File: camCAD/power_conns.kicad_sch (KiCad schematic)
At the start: 3 parts, among them J3 BATTERY

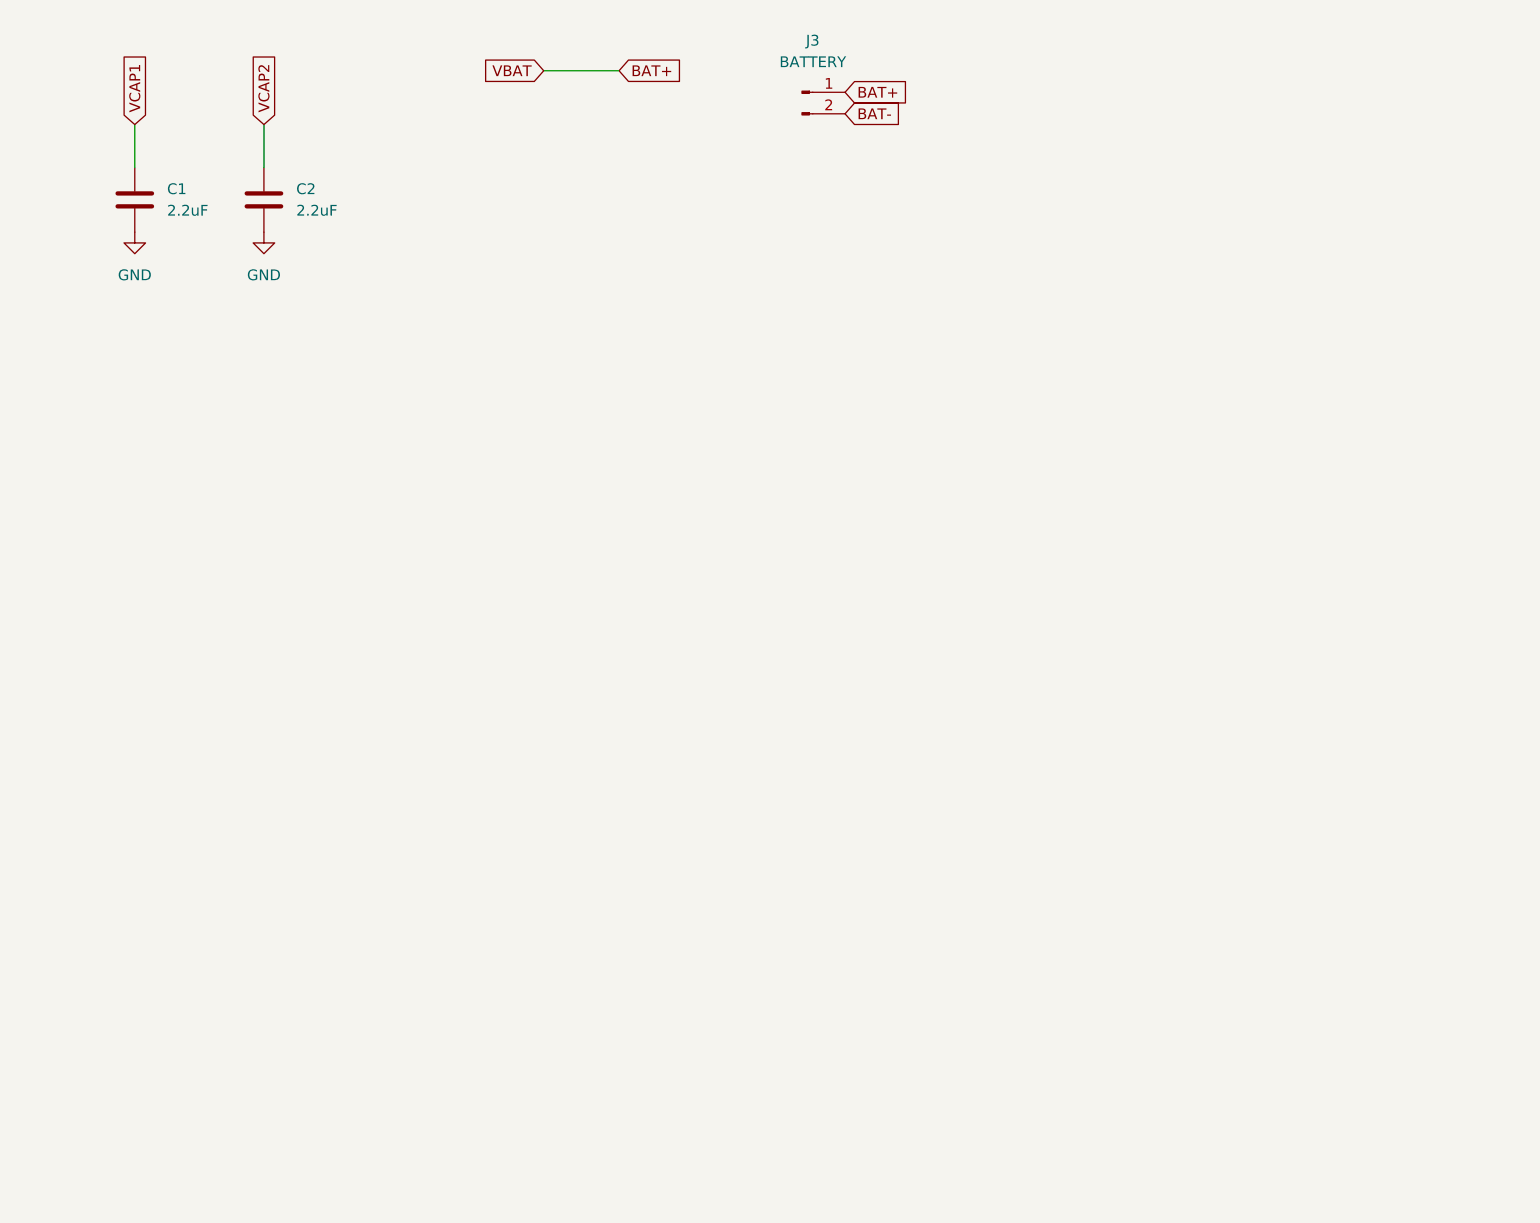
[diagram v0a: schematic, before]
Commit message: Included buck converter schematic
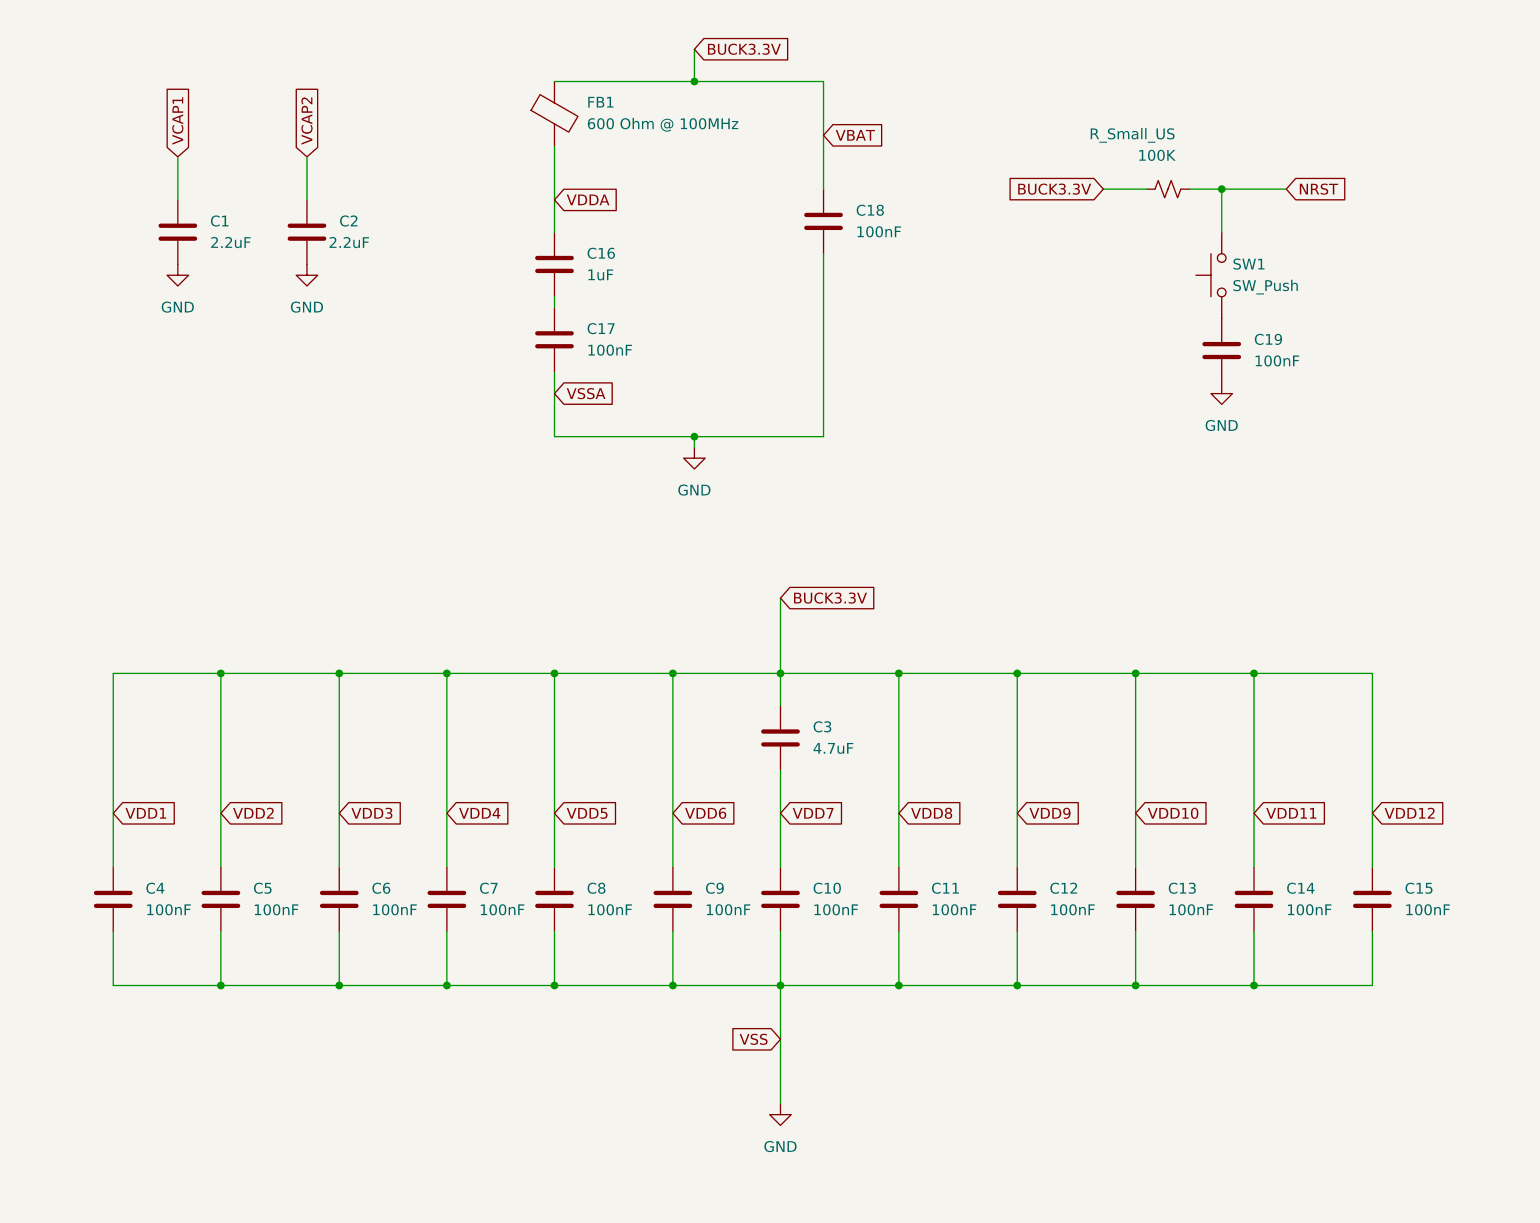
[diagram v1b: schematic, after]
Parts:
- removed J3: BATTERY, symbol Connector:Conn_01x02_Pin
- added 100K: R_Small_US, symbol Device:R_Small_US
- added C10, C11, C12, C13, C14, C15, C17, C18, C19, C4, C5, C6, C7, C8, C9: 100nF, symbol Device:C
- added C16: 1uF, symbol Device:C
- added C3: 4.7uF, symbol Device:C
- added FB1: 600 Ohm @ 100MHz, symbol Device:FerriteBead
- added SW1: SW_Push, symbol Switch:SW_Push
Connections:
- net GND: now also C10.2, C11.2, C12.2, C13.2, C14.2, C15.2, C17.2, C18.2, C19.2, C4.2, C5.2, C6.2, C7.2, C8.2, C9.2
- new net: C19.1, SW1.1
- new net: C16.2, C17.1
- new net BUCK3.3V: 100K.1, C11.1, C12.1, C13.1, C14.1, C15.1, C18.1, C3.1, C4.1, C5.1, C6.1, C7.1, C8.1, C9.1, FB1.1
- new net NRST: 100K.2, SW1.2
- new net VDD7: C10.1, C3.2
- new net VDDA: C16.1, FB1.2
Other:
- title: (none) -> Power Connections for Camera system
- moved on the sheet: C1, C2

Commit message: restructured hierarchy and cleaned up schematic
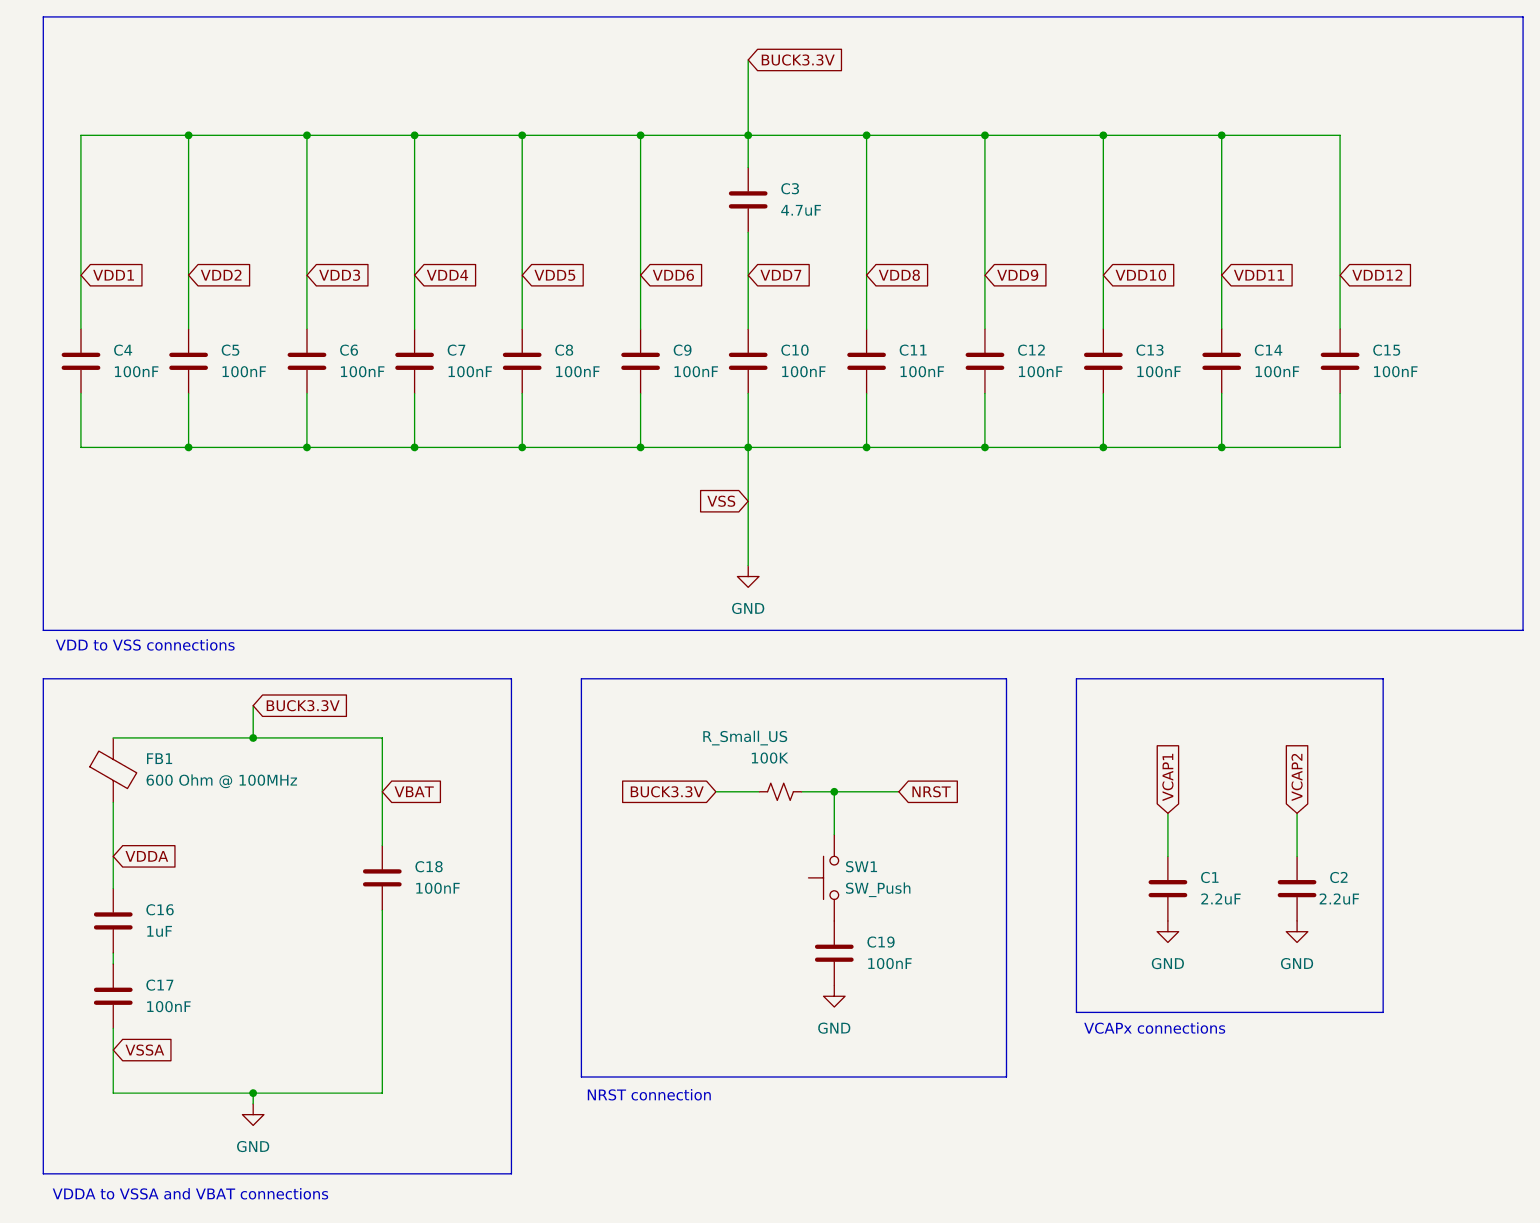
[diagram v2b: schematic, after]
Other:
- note added: "NRST connection"
- note added: "VCAPx connections"
- note added: "VDD to VSS connections"
- note added: "VDDA to VSSA and VBAT connections"
- moved on the sheet: 100K, C1, C10, C11, C12, C13, C14, C15, C16, C17, C18, C19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

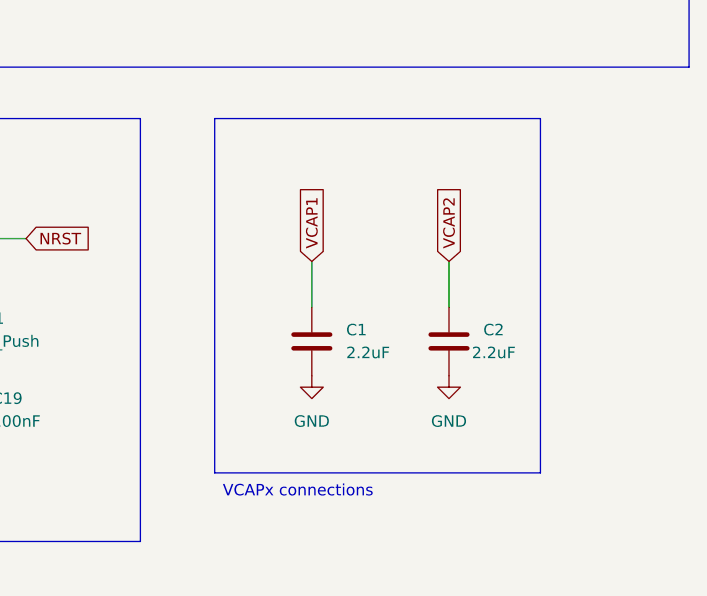
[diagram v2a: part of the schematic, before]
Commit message: Added battery to HardwareNotes.md, some touch ups on schematic
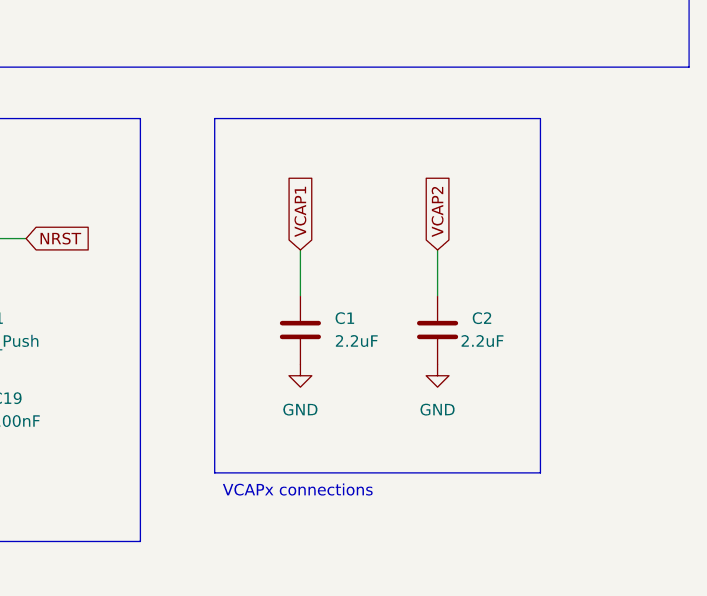
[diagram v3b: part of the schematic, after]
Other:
- moved on the sheet: C1, C2
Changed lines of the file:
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@@
 	(wire
 		(pts
-			(xy 162.56 109.22) (xy 162.56 114.3)
+			(xy 161.29 107.95) (xy 161.29 113.03)
 		)
 		(stroke
@@
 	(wire
 		(pts
-			(xy 147.32 109.22) (xy 147.32 114.3)
+			(xy 146.05 107.95) (xy 146.05 113.03)
 		)
 		(stroke
@@
 	(global_label "VCAP1"
 		(shape input)
-		(at 147.32 109.22 90)
+		(at 146.05 107.95 90)
 		(fields_autoplaced yes)
 		(effects
@@
 		)
 		(property "Intersheetrefs" "${INTERSHEET_REFS}"
-			(at 147.32 100.3081 90)
+			(at 146.05 99.0381 90)
 			(hide yes)
 			(show_name no)
@@
 	(global_label "VCAP2"
 		(shape input)
-		(at 162.56 109.22 90)
+		(at 161.29 107.95 90)
 		(fields_autoplaced yes)
 		(effects
@@
 		)
 		(property "Intersheetrefs" "${INTERSHEET_REFS}"
-			(at 162.56 100.3081 90)
+			(at 161.29 99.0381 90)
 			(hide yes)
 			(show_name no)
@@
 	(symbol
 		(lib_id "power:GND")
-		(at 162.56 121.92 0)
+		(at 161.29 120.65 0)
 		(unit 1)
 		(body_style 1)
@@
 		(fields_autoplaced yes)
 		(property "Reference" "#PWR010"
-			(at 162.56 128.27 0)
+			(at 161.29 127 0)
 			(hide yes)
 			(show_name no)
@@
 		)
 		(property "Value" "GND"
-			(at 162.56 127 0)
+			(at 161.29 125.73 0)
 			(show_name no)
 			(do_not_autoplace no)
@@
 		)
 		(property "Footprint" ""
-			(at 162.56 121.92 0)
+			(at 161.29 120.65 0)
 			(hide yes)
 			(show_name no)
@@
 		)
 		(property "Datasheet" ""
-			(at 162.56 121.92 0)
+			(at 161.29 120.65 0)
 			(hide yes)
 			(show_name no)
@@
 		)
 		(property "Description" "Power symbol creates a global label with name \"GND\" , ground"
-			(at 162.56 121.92 0)
+			(at 161.29 120.65 0)
 			(hide yes)
 			(show_name no)
@@
 	(symbol
 		(lib_id "Device:C")
-		(at 147.32 118.11 0)
+		(at 146.05 116.84 0)
 		(unit 1)
 		(body_style 1)
@@
 		(fields_autoplaced yes)
 		(property "Reference" "C1"
-			(at 151.13 116.8399 0)
+			(at 149.86 115.5699 0)
 			(show_name no)
 			(do_not_autoplace no)
@@
 		)
 		(property "Value" "2.2uF"
-			(at 151.13 119.3799 0)
+			(at 149.86 118.1099 0)
 			(show_name no)
 			(do_not_autoplace no)
@@
 		)
 		(property "Footprint" ""
-			(at 148.2852 121.92 0)
+			(at 147.0152 120.65 0)
 			(hide yes)
 			(show_name no)
@@
 		)
 		(property "Datasheet" ""
-			(at 147.32 118.11 0)
+			(at 146.05 116.84 0)
 			(hide yes)
 			(show_name no)
@@
 		)
 		(property "Description" "Unpolarized capacitor"
-			(at 147.32 118.11 0)
+			(at 146.05 116.84 0)
 			(hide yes)
 			(show_name no)
@@
 	(symbol
 		(lib_id "Device:C")
-		(at 162.56 118.11 0)
+		(at 161.29 116.84 0)
 		(unit 1)
 		(body_style 1)
@@
 		(dnp no)
 		(property "Reference" "C2"
-			(at 166.37 116.8399 0)
+			(at 165.1 115.5699 0)
 			(show_name no)
 			(do_not_autoplace no)
@@
 		)
 		(property "Value" "2.2uF"
-			(at 165.1 119.3799 0)
+			(at 163.83 118.1099 0)
 			(show_name no)
 			(do_not_autoplace no)
@@
 		)
 		(property "Footprint" ""
-			(at 163.5252 121.92 0)
+			(at 162.2552 120.65 0)
 			(hide yes)
 			(show_name no)
@@
 		)
 		(property "Datasheet" ""
-			(at 162.56 118.11 0)
+			(at 161.29 116.84 0)
 			(hide yes)
 			(show_name no)
@@
 		)
 		(property "Description" "Unpolarized capacitor"
-			(at 162.56 118.11 0)
+			(at 161.29 116.84 0)
 			(hide yes)
 			(show_name no)
@@
 	(symbol
 		(lib_id "power:GND")
-		(at 147.32 121.92 0)
+		(at 146.05 120.65 0)
 		(unit 1)
 		(body_style 1)
@@
 		(fields_autoplaced yes)
 		(property "Reference" "#PWR09"
-			(at 147.32 128.27 0)
+			(at 146.05 127 0)
 			(hide yes)
 			(show_name no)
@@
 		)
 		(property "Value" "GND"
-			(at 147.32 127 0)
+			(at 146.05 125.73 0)
 			(show_name no)
 			(do_not_autoplace no)
@@
 		)
 		(property "Footprint" ""
-			(at 147.32 121.92 0)
+			(at 146.05 120.65 0)
 			(hide yes)
 			(show_name no)
@@
 		)
 		(property "Datasheet" ""
-			(at 147.32 121.92 0)
+			(at 146.05 120.65 0)
 			(hide yes)
 			(show_name no)
@@
 		)
 		(property "Description" "Power symbol creates a global label with name \"GND\" , ground"
-			(at 147.32 121.92 0)
-			(hide yes)
-			(show_name no)
+			(at 146.05 120.65 0)
+			(hide yes)
+			(show_name no)
